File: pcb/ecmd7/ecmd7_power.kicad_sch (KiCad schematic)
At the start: 77 parts, among them Q10 BSC098N10NS5, Q7 BSC098N10NS5, Q8 BSC098N10NS5, Q9 BSC098N10NS5, U14 LM5118MH, U3 LM5118MH, U6 TLV71318PDBV, U8 TLV803EA30DBZ, U9 LT1616ES6#TRPBF

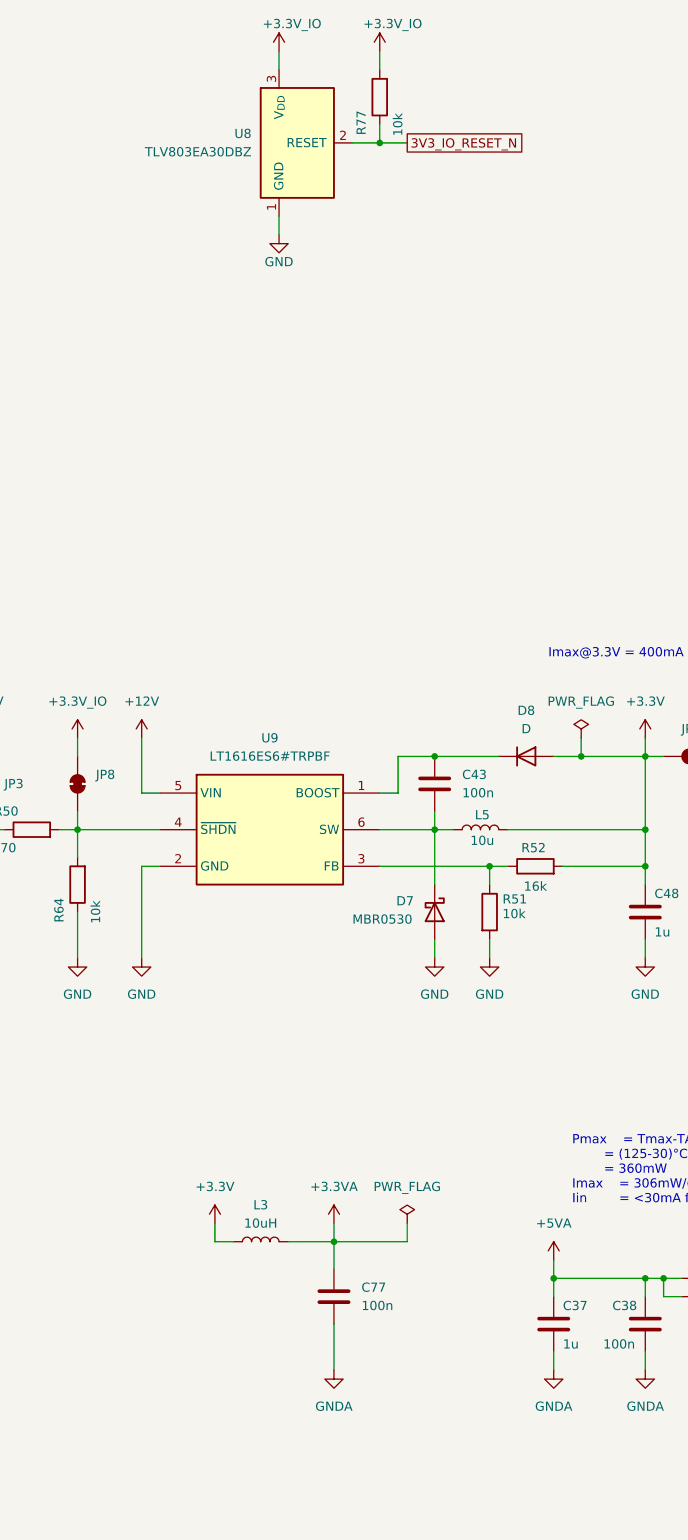
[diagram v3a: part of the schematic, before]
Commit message: Routing complete, DRC successful
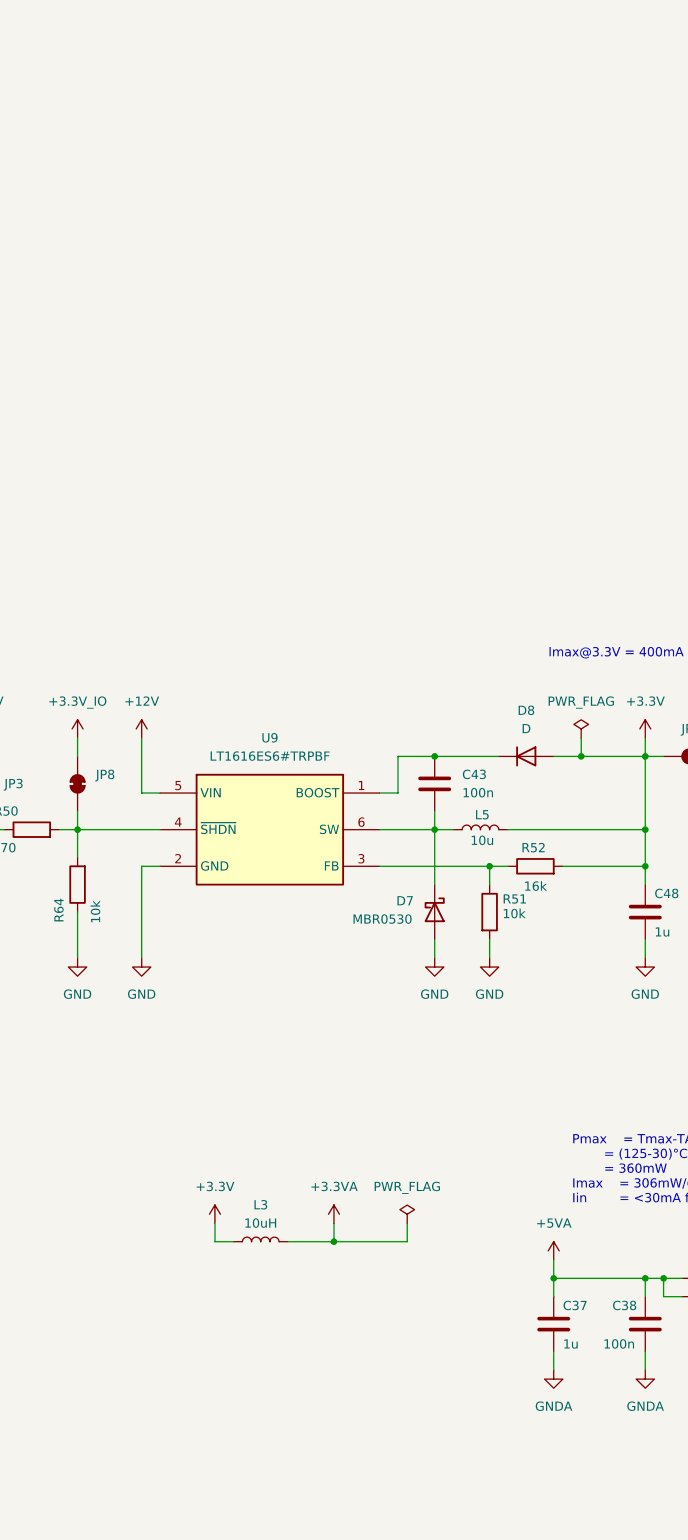
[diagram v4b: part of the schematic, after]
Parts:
- removed C77: 100n, Capacitor_SMD:C_0805_2012Metric, symbol Device:C
- removed R77: 10k, Resistor_SMD:R_0805_2012Metric, symbol Device:R
- removed U8: TLV803EA30DBZ, Package_TO_SOT_SMD:SOT-23, symbol Power_Supervisor:TLV810EA29DBZ

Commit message: Final layout
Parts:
- removed D8: D, Diode_SMD:D_MiniMELF, symbol Device:D
- added D23: LL4148, Diode_SMD:D_MiniMELF, symbol Diode:LL4148
- C37, C48: value 1u -> 1u/25V
- JP3, JP9: value SolderJumper_2_Open -> INT
- JP8: value SolderJumper_2_Bridged -> EXT
- L3: value 10uH -> 10u
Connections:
- net +3.3V: now also D23.2 (A)
- net at C43.1, U9.1 (BOOST): now also D23.1 (K)
